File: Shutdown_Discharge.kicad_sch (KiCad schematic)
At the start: 21 parts, among them J27 DISCHARGE_RELAY, K1 EX12U1S, Q12 2N7002NXAKR, Q13 2N7002NXAKR, Q14 NTR5105PT1G, Q15 2N7002NXAK

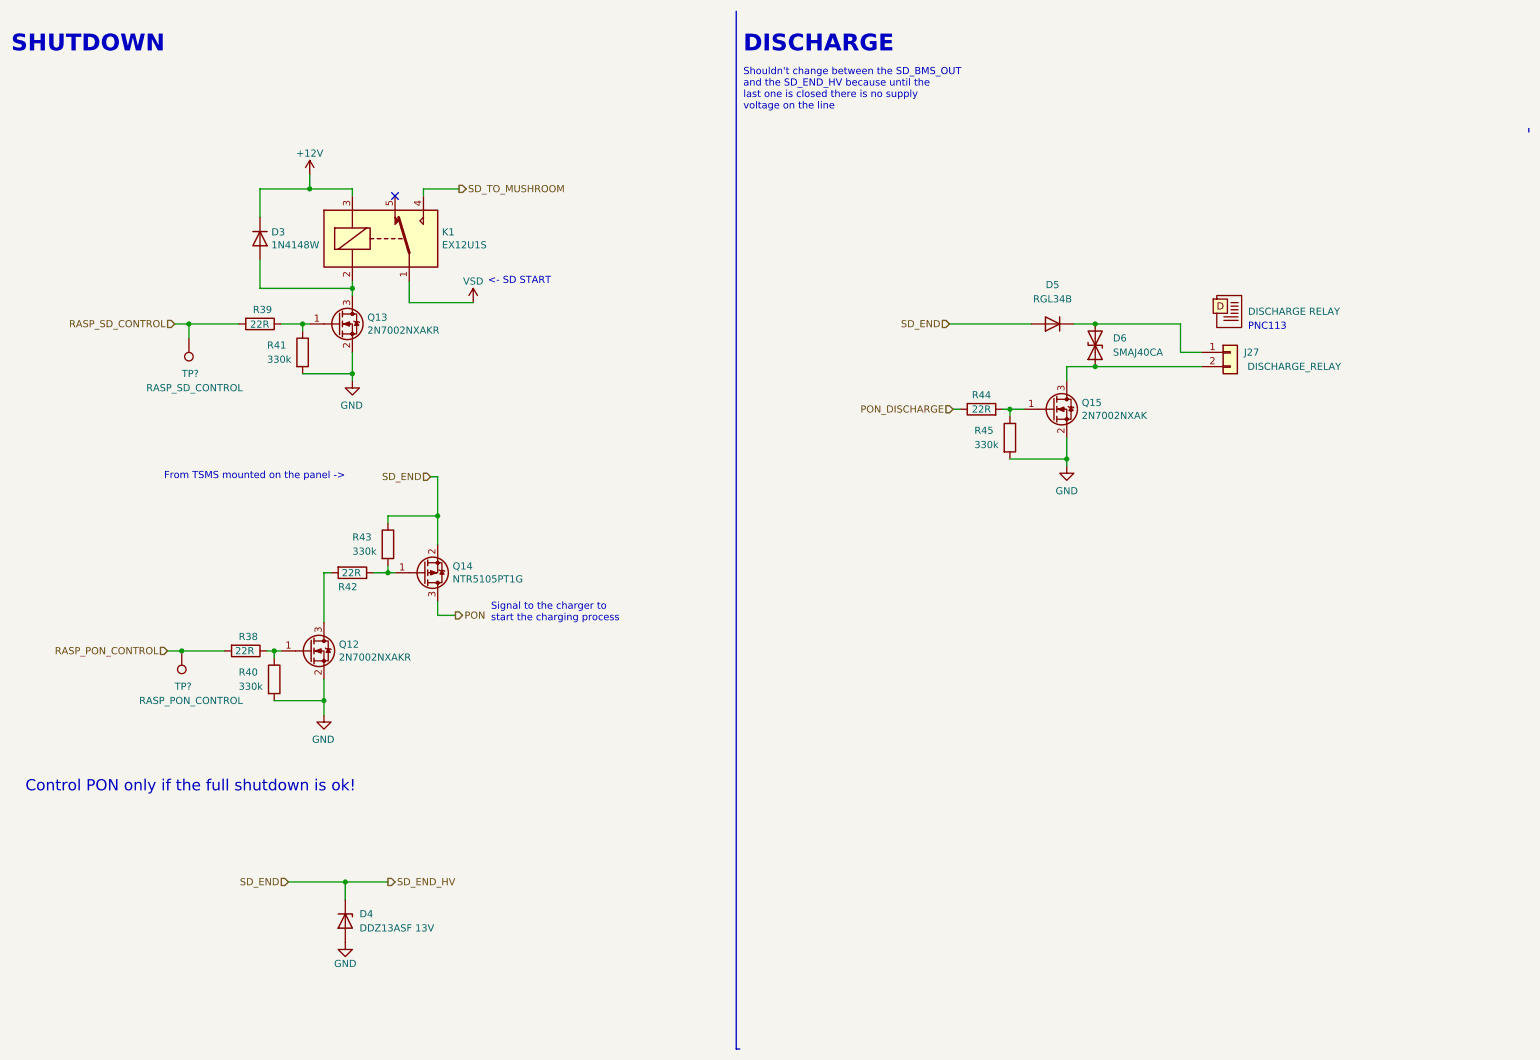
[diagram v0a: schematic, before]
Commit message: modified schematic and started design pcb
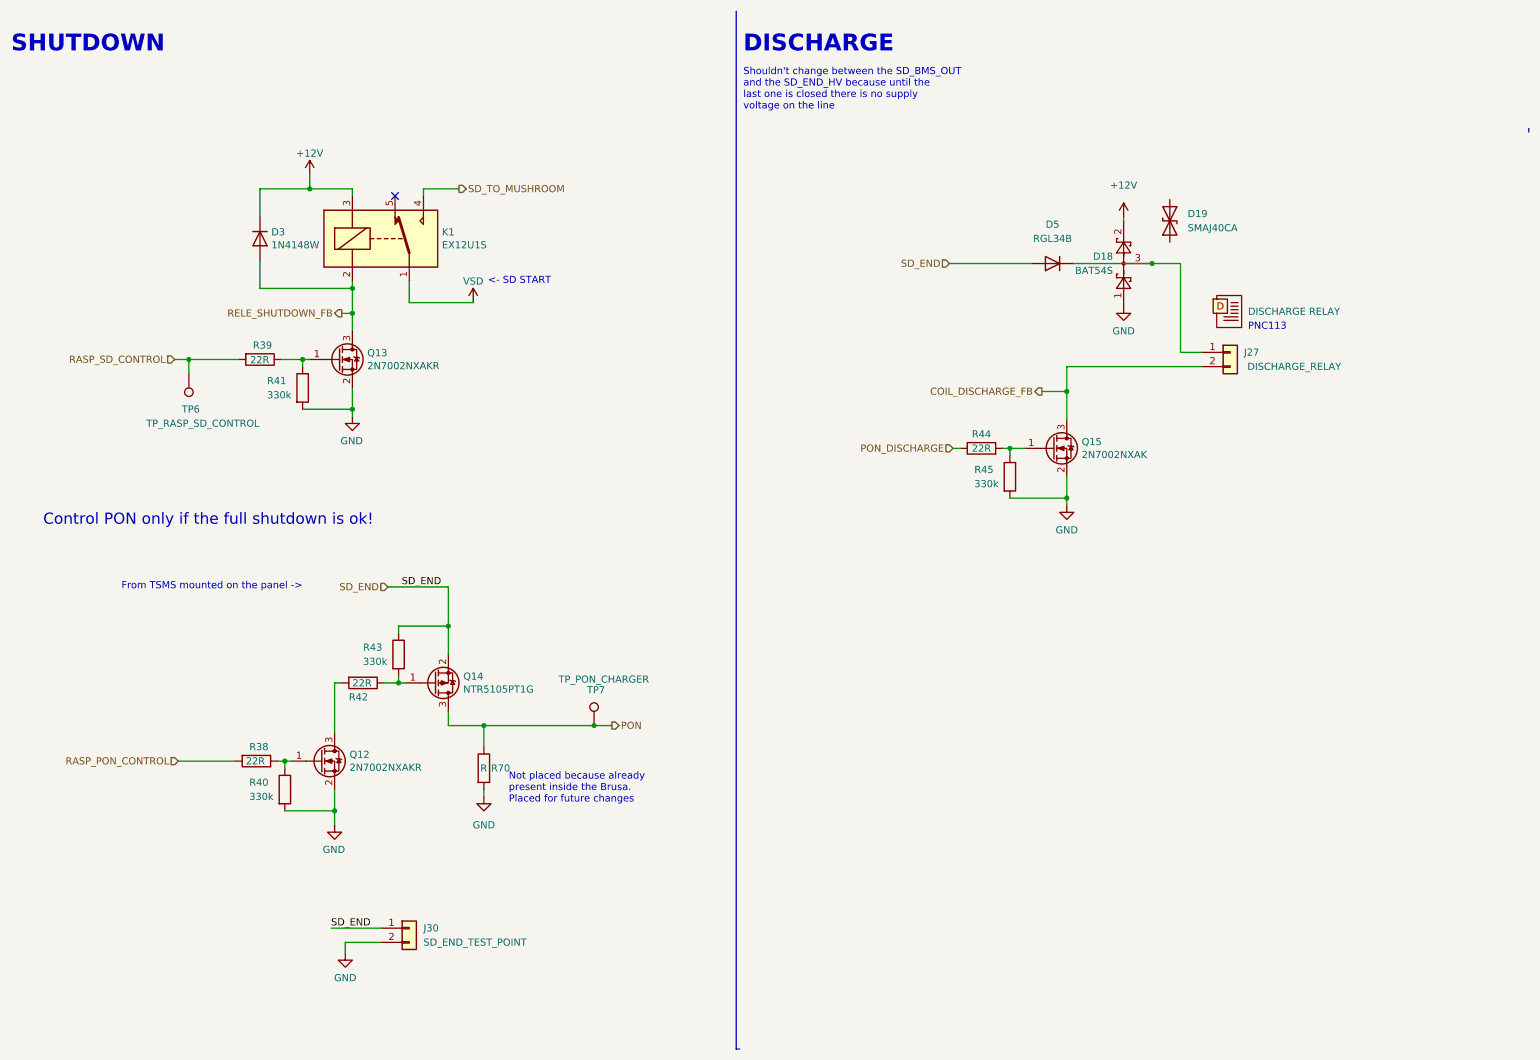
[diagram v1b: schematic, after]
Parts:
- removed D4: DDZ13ASF 13V, Diode_SMD:D_SOD-323F, symbol Device:D_Zener
- removed D6: SMAJ40CA, Diode_SMD:D_SMA, symbol Device:D_TVS
- removed TP?: RASP_PON_CONTROL, symbol Connector:TestPoint
- added D18: BAT54S, Package_TO_SOT_SMD:SOT-23, symbol Diode:BAT54S
- added D19: SMAJ40CA, Diode_SMD:D_SMA, symbol Device:D_TVS
- added J30: SD_END_TEST_POINT, Connector_Molex:Molex_Micro-Fit_3.0_43650-0215_1x02_P3.00mm_Vertical, symbol Connector_Generic:Conn_01x02
- added R70: R, Resistor_SMD:R_0805_2012Metric, symbol Device:R
- added TP7: TP_PON_CHARGER, TestPoint:TestPoint_Pad_D2.0mm, symbol Connector:TestPoint
- TP6: renamed from TP?; value RASP_SD_CONTROL -> TP_RASP_SD_CONTROL; footprint (none) -> TestPoint:TestPoint_Pad_D2.0mm
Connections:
- net +12V: now also D18.2
- net GND: now also D18.1, J30.2 (Pin_2), R70.2
- net PON: now also R70.1, TP7.1
- net SD_END: now also J30.1 (Pin_1)
- net RELE_SHUTDOWN_FB: now reaches D3.2 (A), K1.2, Q13.3 (D)
- net at D5.1 (K), J27.1 (Pin_1): now also D18.3
- net COIL_DISCHARGE_FB: now reaches J27.2 (Pin_2), Q15.3 (D)
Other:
- note added: "Not placed because already present inside the Brusa. Placed for future changes"
- note removed: "Signal to the charger to start the charging process"
- moved on the sheet: D5, Q12, Q13, Q14, Q15, R38, R39, R40, R41, R42, R43, R44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

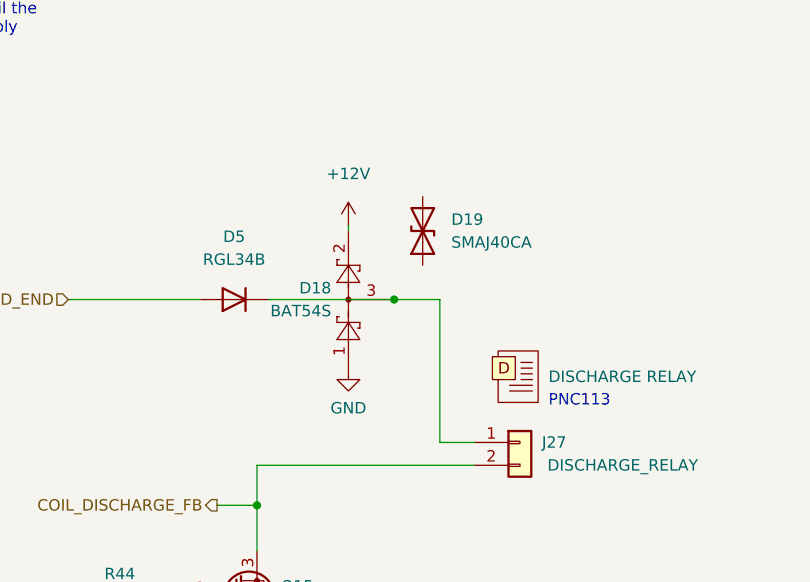
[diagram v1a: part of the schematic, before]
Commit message: Fixed frequency of LPF, added reverse polarity protection
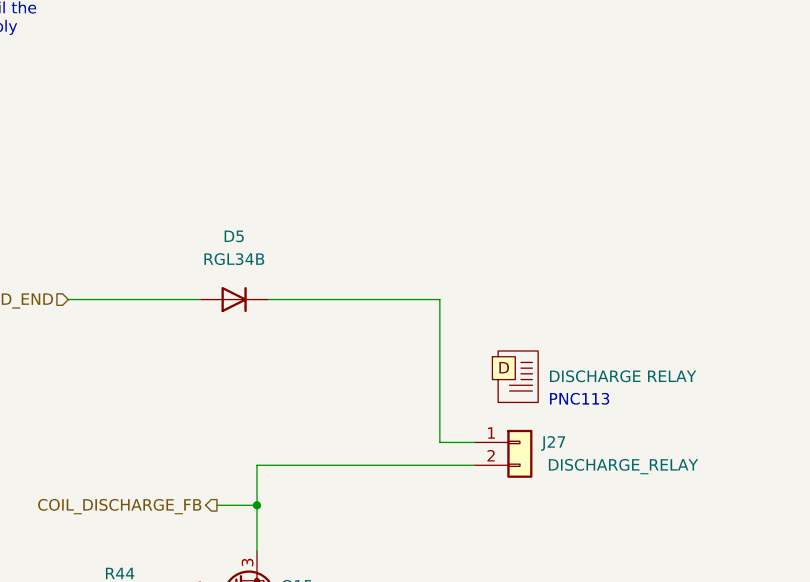
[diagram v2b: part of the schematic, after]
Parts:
- removed D18: BAT54S, Package_TO_SOT_SMD:SOT-23, symbol Diode:BAT54S
- removed D19: SMAJ40CA, Diode_SMD:D_SMA, symbol Device:D_TVS
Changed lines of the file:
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@@
   (junction (at 74.93 62.23) (diameter 0) (color 0 0 0 0)
-  )
-  (junction (at 217.805 57.785) (diameter 0) (color 0 0 0 0)
   )
   (junction (at 74.93 83.82) (diameter 0) (color 0 0 0 0)
@@
     (stroke (width 0) (type default) (color 0 0 0 0))
   )
-  (wire (pts (xy 212.725 49.53) (xy 212.725 50.165))
-    (stroke (width 0) (type default) (color 0 0 0 0))
-  )
   (wire (pts (xy 202.565 99.695) (xy 202.565 100.965))
     (stroke (width 0) (type default) (color 0 0 0 0))
@@
     (stroke (width 0) (type default) (color 0 0 0 0))
   )
-  (wire (pts (xy 217.805 57.785) (xy 222.885 57.785))
-    (stroke (width 0) (type default) (color 0 0 0 0))
-  )
   (wire (pts (xy 92.075 115.57) (xy 92.075 122.555))
     (stroke (width 0) (type default) (color 0 0 0 0))
@@
     (stroke (width 0) (type default) (color 0 0 0 0))
   )
-  (wire (pts (xy 203.835 57.785) (xy 217.805 57.785))
+  (wire (pts (xy 203.835 57.785) (xy 222.885 57.785))
     (stroke (width 0) (type default) (color 0 0 0 0))
   )
@@
     (pin "2")
   )
-  (symbol (lib_id "power:+12V") (at 212.725 49.53 0) (unit 1)
-    (in_bom yes) (on_board yes) (fields_autoplaced)
-    (property "Reference" "#PWR0171" (id 0) (at 212.725 53.34 0)
-      (effects (font (size 1.27 1.27)) hide)
-    )
-    (property "Value" "+12V" (id 1) (at 212.725 43.815 0))
-    (property "Footprint" "" (id 2) (at 212.725 49.53 0)
-      (effects (font (size 1.27 1.27)) hide)
-    )
-    (property "Datasheet" "" (id 3) (at 212.725 49.53 0)
-      (effects (font (size 1.27 1.27)) hide)
-    )
-    (pin "1")
-  )
   (symbol (lib_id "power:GND") (at 74.93 85.09 0) (mirror y) (unit 1)
     (in_bom yes) (on_board yes)
@@
     (pin "2")
   )
-  (symbol (lib_id "Device:D_TVS") (at 220.98 50.165 90) (unit 1)
-    (in_bom yes) (on_board yes) (fields_autoplaced)
-    (property "Reference" "D19" (id 0) (at 224.155 48.8949 90)
-      (effects (font (size 1.27 1.27)) (justify right))
-    )
-    (property "Value" "SMAJ40CA" (id 1) (at 224.155 51.4349 90)
-      (effects (font (size 1.27 1.27)) (justify right))
-    )
-    (property "Footprint" "Diode_SMD:D_SMA" (id 2) (at 220.98 50.165 0)
-      (effects (font (size 1.27 1.27)) hide)
-    )
-    (property "Datasheet" "datasheets/SMAJ-778033.pdf" (id 3) (at 220.98 50.165 0)
-      (effects (font (size 1.27 1.27)) hide)
-    )
-    (pin "1")
-    (pin "2")
-  )
-  (symbol (lib_id "power:GND") (at 212.725 65.405 0) (unit 1)
-    (in_bom yes) (on_board yes) (fields_autoplaced)
-    (property "Reference" "#PWR0170" (id 0) (at 212.725 71.755 0)
-      (effects (font (size 1.27 1.27)) hide)
-    )
-    (property "Value" "GND" (id 1) (at 212.725 69.85 0))
-    (property "Footprint" "" (id 2) (at 212.725 65.405 0)
-      (effects (font (size 1.27 1.27)) hide)
-    )
-    (property "Datasheet" "" (id 3) (at 212.725 65.405 0)
-      (effects (font (size 1.27 1.27)) hide)
-    )
-    (pin "1")
-  )
-  (symbol (lib_id "Diode:BAT54S") (at 212.725 57.785 90) (unit 1)
-    (in_bom yes) (on_board yes) (fields_autoplaced)
-    (property "Reference" "D18" (id 0) (at 210.82 56.5149 90)
-      (effects (font (size 1.27 1.27)) (justify left))
-    )
-    (property "Value" "BAT54S" (id 1) (at 210.82 59.0549 90)
-      (effects (font (size 1.27 1.27)) (justify left))
-    )
-    (property "Footprint" "Package_TO_SOT_SMD:SOT-23" (id 2) (at 209.55 55.88 0)
-      (effects (font (size 1.27 1.27)) (justify left) hide)
-    )
-    (property "Datasheet" "https://www.diodes.com/assets/Datasheets/ds11005.pdf" (id 3) (at 212.725 60.833 0)
-      (effects (font (size 1.27 1.27)) hide)
-    )
-    (pin "1")
-    (pin "2")
-    (pin "3")
-  )
 )

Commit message: First version of the pcb layout
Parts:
- J27: footprint Connector_Molex:Molex_Micro-Fit_3.0_43650-0200_1x02_P3.00mm_Horizontal -> Connector_Molex:Molex_Micro-Fit_3.0_43650-0215_1x02_P3.00mm_Vertical
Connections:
- net +12V is gone; now on net VCC: D3.1 (K), K1.3
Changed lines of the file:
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@@
     (property "Reference" "J27" (id 0) (at 235.585 73.66 0))
     (property "Value" "DISCHARGE_RELAY" (id 1) (at 243.205 76.2 0))
-    (property "Footprint" "Connector_Molex:Molex_Micro-Fit_3.0_43650-0200_1x02_P3.00mm_Horizontal" (id 2) (at 231.775 73.66 0)
+    (property "Footprint" "Connector_Molex:Molex_Micro-Fit_3.0_43650-0215_1x02_P3.00mm_Vertical" (id 2) (at 231.775 73.66 0)
       (effects (font (size 1.27 1.27)) hide)
     )
@@
     (pin "2")
   )
-  (symbol (lib_id "power:+12V") (at 67.31 41.91 0) (unit 1)
-    (in_bom yes) (on_board yes)
-    (property "Reference" "#PWR083" (id 0) (at 67.31 45.72 0)
+  (symbol (lib_id "Eagle_Main:VSD") (at 67.31 41.91 0) (unit 1)
+    (in_bom no) (on_board no) (fields_autoplaced)
+    (property "Reference" "#PWR0148" (id 0) (at 67.31 45.72 0)
       (effects (font (size 1.27 1.27)) hide)
     )
-    (property "Value" "+12V" (id 1) (at 67.31 38.1 0))
+    (property "Value" "VSD" (id 1) (at 67.31 36.83 0))
     (property "Footprint" "" (id 2) (at 67.31 41.91 0)
       (effects (font (size 1.27 1.27)) hide)

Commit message: Fixed Schematic, fixed some traces. Still not finished
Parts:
- TP6: value TP_RASP_SD_CONTROL -> RASPI_SD
- TP7: value TP_PON_CHARGER -> PON
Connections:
- net RELE_SHUTDOWN_FB renamed RELAY_SHUTDOWN_FB
- net VCC renamed VSD
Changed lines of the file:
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@@
     (stroke (width 0) (type default) (color 0 0 0 0))
   )
-  (wire (pts (xy 73.025 66.675) (xy 74.93 66.675))
+  (wire (pts (xy 71.12 66.675) (xy 74.93 66.675))
     (stroke (width 0) (type default) (color 0 0 0 0))
   )
@@
   )
   (text "Not placed because already\npresent inside the Brusa.\nPlaced for future changes"
-    (at 102.87 154.305 0)
+    (at 101.6 156.21 0)
     (effects (font (size 1.27 1.27)) (justify left bottom))
   )
@@
     (effects (font (size 1.27 1.27)) (justify right))
   )
-  (hierarchical_label "RELE_SHUTDOWN_FB" (shape output) (at 73.025 66.675 180)
+  (hierarchical_label "RELAY_SHUTDOWN_FB" (shape output) (at 71.12 66.675 180)
     (effects (font (size 1.27 1.27)) (justify right))
   )
@@
     (pin "1")
   )
+  (symbol (lib_name "VSD_1") (lib_id "Eagle_Main:VSD") (at 67.31 41.91 0) (unit 1)
+    (in_bom no) (on_board no)
+    (property "Reference" "#PWR0148" (id 0) (at 67.31 45.72 0)
+      (effects (font (size 1.27 1.27)) hide)
+    )
+    (property "Value" "VSD" (id 1) (at 67.31 38.1 0))
+    (property "Footprint" "" (id 2) (at 67.31 41.91 0)
+      (effects (font (size 1.27 1.27)) hide)
+    )
+    (property "Datasheet" "" (id 3) (at 67.31 41.91 0)
+      (effects (font (size 1.27 1.27)) hide)
+    )
+    (pin "1")
+  )
   (symbol (lib_id "Device:R") (at 58.42 74.93 270) (unit 1)
     (in_bom yes) (on_board yes)
@@
     )
     (property "Datasheet" "" (id 3) (at 74.93 85.09 0)
+      (effects (font (size 1.27 1.27)) hide)
+    )
+    (pin "1")
+  )
+  (symbol (lib_name "VSD_1") (lib_id "Eagle_Main:VSD") (at 96.52 64.77 0) (unit 1)
+    (in_bom no) (on_board no)
+    (property "Reference" "#PWR0174" (id 0) (at 96.52 68.58 0)
+      (effects (font (size 1.27 1.27)) hide)
+    )
+    (property "Value" "VSD" (id 1) (at 96.52 60.96 0))
+    (property "Footprint" "" (id 2) (at 96.52 64.77 0)
+      (effects (font (size 1.27 1.27)) hide)
+    )
+    (property "Datasheet" "" (id 3) (at 96.52 64.77 0)
       (effects (font (size 1.27 1.27)) hide)
     )
@@
       (effects (font (size 1.27 1.27)) (justify right))
     )
-    (property "Value" "TP_RASP_SD_CONTROL" (id 1) (at 38.1 86.36 0)
+    (property "Value" "RASPI_SD" (id 1) (at 41.275 85.725 0)
       (effects (font (size 1.27 1.27)) (justify right))
     )
@@
     (pin "2")
   )
-  (symbol (lib_id "Eagle_Main:VSD") (at 96.52 64.77 0) (unit 1)
-    (in_bom no) (on_board no)
-    (property "Reference" "#PWR087" (id 0) (at 96.52 68.58 0)
-      (effects (font (size 1.27 1.27)) hide)
-    )
-    (property "Value" "VSD" (id 1) (at 96.52 60.96 0))
-    (property "Footprint" "" (id 2) (at 96.52 64.77 0)
-      (effects (font (size 1.27 1.27)) hide)
-    )
-    (property "Datasheet" "" (id 3) (at 96.52 64.77 0)
-      (effects (font (size 1.27 1.27)) hide)
-    )
-    (pin "1")
-  )
   (symbol (lib_id "Device:R") (at 57.785 146.685 270) (unit 1)
     (in_bom yes) (on_board yes)
@@
   (symbol (lib_id "Connector:TestPoint") (at 118.11 140.335 0) (mirror y) (unit 1)
     (in_bom yes) (on_board yes)
-    (property "Reference" "TP7" (id 0) (at 116.84 133.985 0)
+    (property "Reference" "TP7" (id 0) (at 116.84 132.715 0)
       (effects (font (size 1.27 1.27)) (justify right))
     )
-    (property "Value" "TP_PON_CHARGER" (id 1) (at 111.76 132.08 0)
+    (property "Value" "PON" (id 1) (at 116.205 134.62 0)
       (effects (font (size 1.27 1.27)) (justify right))
     )
@@
     (pin "2")
   )
-  (symbol (lib_id "Eagle_Main:VSD") (at 67.31 41.91 0) (unit 1)
-    (in_bom no) (on_board no) (fields_autoplaced)
-    (property "Reference" "#PWR0148" (id 0) (at 67.31 45.72 0)
-      (effects (font (size 1.27 1.27)) hide)
-    )
-    (property "Value" "VSD" (id 1) (at 67.31 36.83 0))
-    (property "Footprint" "" (id 2) (at 67.31 41.91 0)
-      (effects (font (size 1.27 1.27)) hide)
-    )
-    (property "Datasheet" "" (id 3) (at 67.31 41.91 0)
-      (effects (font (size 1.27 1.27)) hide)
-    )
-    (pin "1")
-  )
   (symbol (lib_id "Device:R") (at 192.405 95.885 0) (unit 1)
